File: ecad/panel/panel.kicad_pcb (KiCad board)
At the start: 4 copper layers, 165.5 x 51.6 mm, 200 parts, among them J2 Conn_01x03_Pin, J3 USB4105-GF-A, J4 5017868090, SW1 SW_SPDT, SW10 SW_SPDT, SW11 SW_SPDT, SW12 SW_SPDT, SW13 SW_SPDT, SW14 SW_SPDT, SW15 SW_SPDT, SW16 SW_SPDT, SW17 SW_Push, SW18 SW_Push, SW19 SW_Push, SW2 SW_SPDT, SW20 SW_Push, SW21 SW_Push, SW22 SW_Push, SW23 SW_Push, SW24 SW_Push, SW25 SW_Push, SW26 SW_Push, SW27 SW_Push, SW28 SW_Push, SW29 SW_Push, SW3 SW_SPDT, SW30 SW_Push, SW31 SW_Push, SW4 SW_SPDT, SW5 SW_SPDT, SW6 SW_SPDT, SW7 SW_SPDT, SW8 SW_SPDT, SW9 SW_SPDT, U1 TLC59211IN, U2 TLC59211IN, U3 TLC59211IN, U4 TLC59211IN, U5 TLC59211IN, U6 RP2350_80QFN, U7 W25Q128JVS, U8 MCP23017_SO, U9 MCP23017_SO, X1 ABM8-272-T3

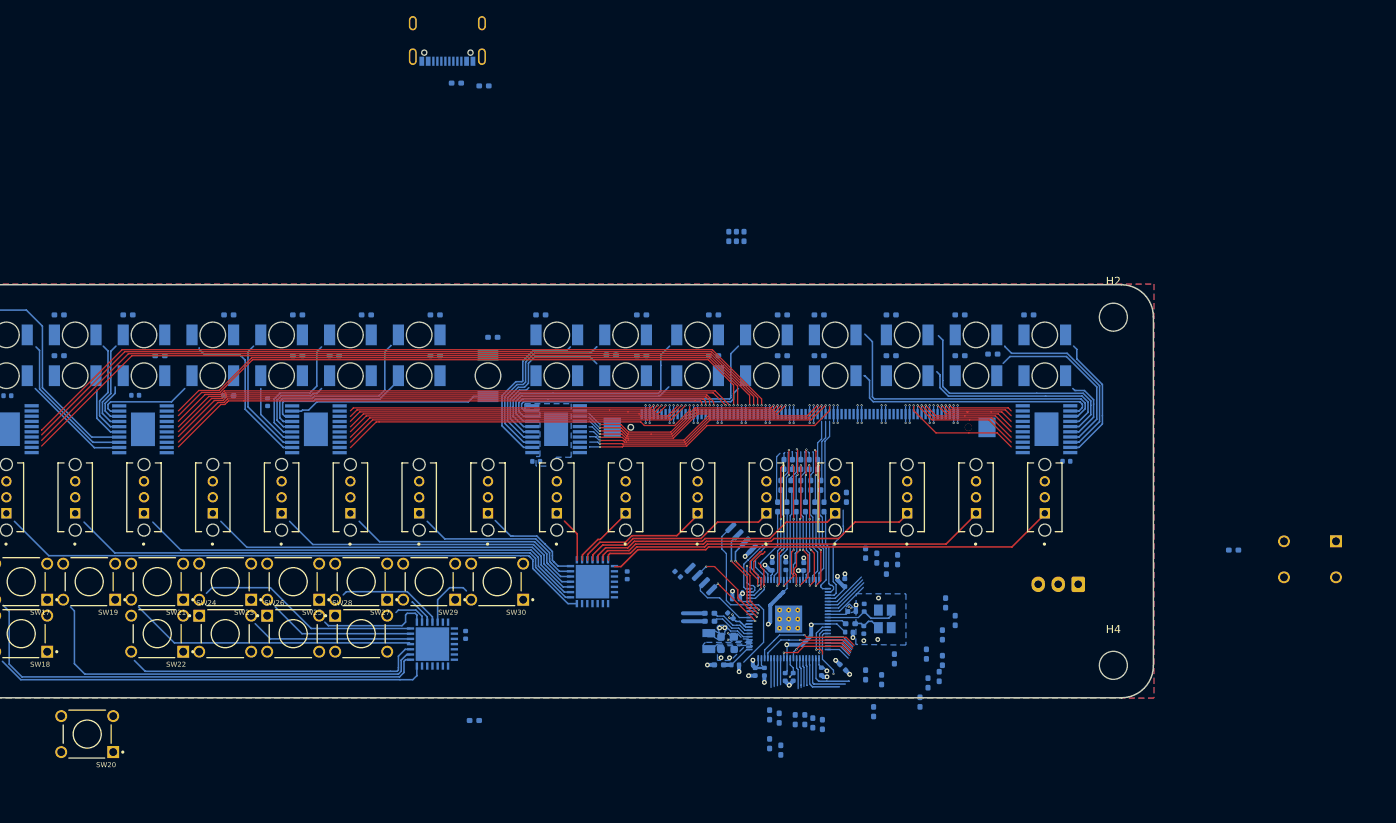
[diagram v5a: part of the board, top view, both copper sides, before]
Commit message: remap changes, various card panel fixes
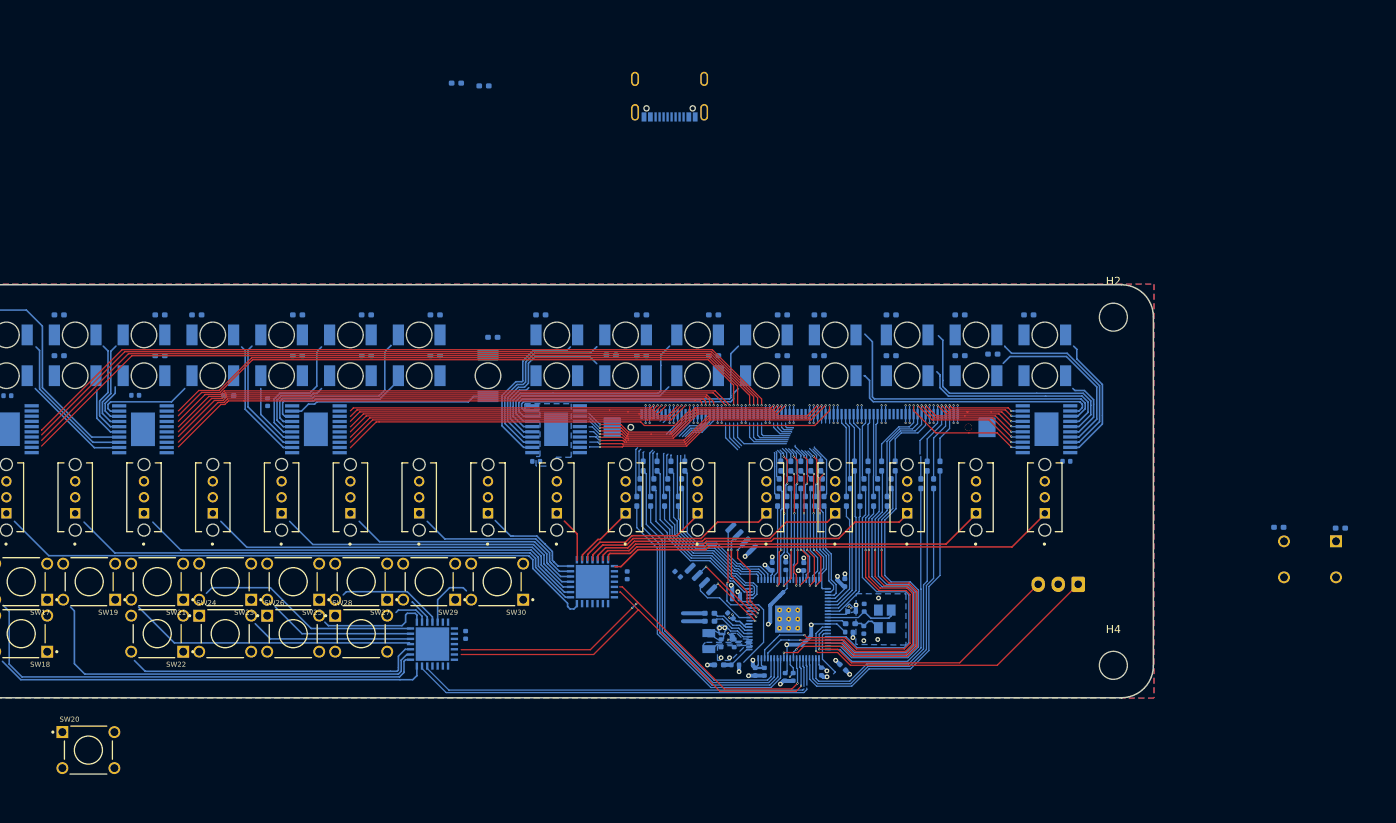
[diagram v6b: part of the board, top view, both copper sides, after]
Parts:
- C7, C8: footprint Capacitor_SMD:C_0603_1608Metric -> Capacitor_SMD:C_0402_1005Metric
- moved R25 110.9 mm to (224.6, 54.2)
- moved R84 37.7 mm to (137.0, 48.7)
- moved R80 36.1 mm to (139.1, 46.5)
- moved R85 35.8 mm to (137.4, 46.5)
- moved R77 35.8 mm to (140.5, 48.7)
- moved R79 35.0 mm to (138.7, 48.7)
- moved R83 34.6 mm to (136.6, 50.9)
- moved R46 33.9 mm to (141.8, 50.9)
- moved R78 33.3 mm to (140.1, 50.9)
- moved R47 31.9 mm to (142.2, 48.7)
- moved R76 31.8 mm to (174.5, 46.5)
- moved R86 30.6 mm to (138.3, 50.9)
- moved R45 29.6 mm to (140.9, 46.5)
- moved J3 28.6 mm to (140.7, -1.90)
- moved R75 27.4 mm to (173.7, 48.7)
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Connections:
- C10 pad 2: +1V1 -> GND
- C11 pad 2: +1V1 -> GND
- J4 pad 10: /BUS10 -> A1
- J4 pad 11: /BUS11 -> D1
- J4 pad 12: /BUS12 -> D0
- J4 pad 16: A0 -> /BUS16
- J4 pad 17: A1 -> /BUS17
- J4 pad 18: A2 -> /BUS18
- J4 pad 21: A3 -> /BUS21
- J4 pad 22: A4 -> /BUS22
- J4 pad 23: A5 -> /BUS23
- J4 pad 24: A6 -> /BUS24
- J4 pad 27: A7 -> /BUS27
- J4 pad 28: D0 -> /BUS28
- J4 pad 29: D1 -> /BUS29
- J4 pad 3: /BUS03 -> A3
- J4 pad 30: D2 -> /BUS30
- J4 pad 33: D3 -> D7
- J4 pad 34: D4 -> D6
- J4 pad 35: D5 -> A6
- J4 pad 36: D6 -> A7
- J4 pad 4: /BUS04 -> D3
- J4 pad 44: A8 -> A4
- J4 pad 45: A9 -> D4
- J4 pad 46: A10 -> A5
- J4 pad 47: A11 -> D5
- J4 pad 5: /BUS05 -> A2
- J4 pad 50: A12 -> PROT
- J4 pad 51: A13 -> INTE
- J4 pad 52: A14 -> WAIT
- J4 pad 53: A15 -> HLDA
- J4 pad 56: INT -> A12
- J4 pad 57: WO -> A13
- J4 pad 58: STACK -> OUT
- J4 pad 59: HLTA -> M1
- J4 pad 6: /BUS06 -> D2
- J4 pad 62: OUT -> A14
- J4 pad 63: M1 -> MEMR
- J4 pad 65: MEMR -> A15
- J4 pad 68: HLDA -> HLTA
- J4 pad 69: WAIT -> STACK
- J4 pad 70: PROT -> A11
- J4 pad 71: INTE -> WO
- J4 pad 74: I2C1_SCK -> A10
- J4 pad 75: I2C1_SDA -> INT
- J4 pad 76: I2C0_SCK -> A9
- J4 pad 77: I2C0_SDA -> A8
- J4 pad 9: /BUS09 -> A0
- R45 pad 2: INTE -> A14
- R46 pad 2: PROT -> MEMR
- R47 pad 2: WAIT -> INP
- R48 pad 2: HLDA -> A15
- R49 pad 2: MEMR -> HLTA
- R50 pad 2: INP -> STACK
- R51 pad 2: M1 -> A11
- R52 pad 2: OUT -> WO
- R53 pad 2: HLTA -> A10
- R54 pad 2: STACK -> INT
- R55 pad 2: WO -> A9
- R56 pad 2: INT -> A8
- R57 pad 2: A15 -> D7
- R58 pad 2: A14 -> D6
- R59 pad 2: A13 -> A6
- R60 pad 2: A12 -> A7
- R61 pad 2: A11 -> D5
- R62 pad 2: A10 -> D4
- R63 pad 2: A9 -> A5
- R64 pad 2: A8 -> A4
- R65 pad 2: D7 -> /BUS30
- R66 pad 2: D6 -> /BUS29
- R67 pad 2: D5 -> /BUS28
- R68 pad 2: D4 -> /BUS27
- R69 pad 2: D3 -> /BUS24
- R70 pad 2: D2 -> /BUS21
- R72 pad 2: D0 -> A0
- R73 pad 2: A7 -> D2
- R74 pad 2: A6 -> A2
- R75 pad 2: A5 -> D3
- R76 pad 2: A4 -> A3
- R77 pad 1: Net-(U6-GPIO36) -> Net-(U6-GPIO0)
- R77 pad 2: A3 -> M1
- R78 pad 1: Net-(U6-GPIO37) -> Net-(U6-GPIO1)
- R78 pad 2: A2 -> OUT
- R79 pad 1: Net-(U6-GPIO38) -> Net-(U6-GPIO2)
- R79 pad 2: A1 -> A12
- R80 pad 1: Net-(U6-GPIO39) -> Net-(U6-GPIO3)
- R80 pad 2: A0 -> A13
- R81 pad 2: /BUS15 -> D0
- R82 pad 2: /BUS12 -> A1
- R83 pad 2: /BUS11 -> PROT
- R84 pad 2: /BUS10 -> INTE
- R85 pad 2: /BUS09 -> WAIT
- R86 pad 2: /BUS06 -> HLDA
- R87 pad 2: /BUS05 -> /BUS22
- R88 pad 2: /BUS04 -> /BUS23
- U1 pad 6: HLDA -> PROT
- U1 pad 7: WAIT -> INTE
- U1 pad 8: PROT -> WAIT
- U1 pad 9: INTE -> HLDA
- U2 pad 2: INT -> A12
- U2 pad 3: WO -> A13
- U2 pad 4: STACK -> OUT
- U2 pad 5: HLTA -> M1
- U2 pad 6: OUT -> A14
- U2 pad 7: M1 -> MEMR
- U2 pad 9: MEMR -> A15
- U3 pad 4: A10 -> INT
- U3 pad 5: A11 -> A10
- U3 pad 6: A12 -> WO
- U3 pad 7: A13 -> A11
- U3 pad 8: A14 -> STACK
- U3 pad 9: A15 -> HLTA
- U4 pad 2: D0 -> A4
- U4 pad 3: D1 -> D4
- U4 pad 4: D2 -> A5
- U4 pad 5: D3 -> D5
- U4 pad 6: D4 -> A7
- U4 pad 7: D5 -> A6
- U5 pad 2: A0 -> D0
- U5 pad 3: A1 -> D1
- U5 pad 4: A2 -> A1
- U5 pad 5: A3 -> A0
- U5 pad 6: A4 -> D2
- U5 pad 7: A5 -> A2
- U5 pad 8: A6 -> D3
- U5 pad 9: A7 -> A3
- U6 pad 15: 3.3V -> GND
- U6 pad 24: 3.3V -> GND
- U6 pad 29: 3.3V -> GND
- U6 pad 41: 3.3V -> GND
- U6 pad 45: Net-(U6-GPIO36) -> unconnected-(U6-GPIO36-Pad45)
- U6 pad 46: Net-(U6-GPIO37) -> unconnected-(U6-GPIO37-Pad46)
- U6 pad 47: Net-(U6-GPIO38) -> I2C1_SDA
- U6 pad 48: Net-(U6-GPIO39) -> I2C1_SCK
- U6 pad 5: 3.3V -> GND
- U6 pad 50: 3.3V -> GND
- U6 pad 68: 3.3V -> GND
- U6 pad 69: 3.3V -> GND
- U6 pad 76: 3.3V -> GND
- U6 pad 77: I2C0_SDA -> Net-(U6-GPIO0)
- U6 pad 78: I2C0_SCK -> Net-(U6-GPIO1)
- U6 pad 79: I2C1_SDA -> Net-(U6-GPIO2)
- U6 pad 80: I2C1_SCK -> Net-(U6-GPIO3)
- U8 pad 12: I2C0_SCK -> /I2C0_SCK
- U8 pad 13: I2C0_SDA -> /I2C0_SDA
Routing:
- net I2C1_SDA: track 44.2 -> 95.8 mm
- net unconnected-(U8-INTA-Pad20): track 0.00 -> 50.0 mm
- net unconnected-(U8-INTB-Pad19): track 0.00 -> 48.6 mm
- net I2C1_SCK: track 48.4 -> 96.1 mm, vias 1 -> 4
- net I2C0_SCK: track 46.4 -> 0.00 mm, vias 2 -> 0
- net I2C0_SDA: track 45.2 -> 0.00 mm, vias 2 -> 0
- net (no net): track 0.00 -> 39.0 mm, vias 0 -> 1
- net A6: track 0.00 -> 37.5 mm, vias 0 -> 2
- net Net-(U6-GPIO44_ADC4): track 3.54 -> 40.3 mm
- net Net-(J2-Pin_1): track 5.04 -> 41.7 mm
- net D7: track 0.00 -> 36.3 mm, vias 0 -> 2
- net Net-(U6-GPIO43_ADC3): track 3.42 -> 39.3 mm
- net Net-(U6-GPIO35): track 7.08 -> 42.8 mm
- net Net-(U6-GPIO31): track 3.15 -> 38.3 mm
- net A4: track 0.00 -> 34.9 mm, vias 0 -> 2
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
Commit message: near-final panel routing
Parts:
- removed the SW20 at (68.0, 82.0)
- added C28: 10u, Capacitor_SMD:C_0402_1005Metric, F.Cu at (102.4, 16.1)
- added C29: 10u, Capacitor_SMD:C_0402_1005Metric, F.Cu at (102.4, 18.1)
- added D37: DEBUG, Diode_SMD:D_0402_1005Metric_Pad0.77x0.64mm_HandSolder, F.Cu at (105.7, 16.1)
- added D41: D_Schottky, Diode_SMD:D_0402_1005Metric, F.Cu at (109.0, 16.1)
- added U10: NCP1117-3.3_SOT223, Package_TO_SOT_SMD:SOT-223-3_TabPin2, B.Cu at (179.0, 61.4)
- moved J2 88.6 mm to (105.2, 42.4), turned to 0 degrees
- moved R16 1.20 mm to (54.6, 37.7), turned to 0 degrees
- moved C10 0.76 mm to (155.2, 72.1), turned to -90 degrees
- moved C16 0.75 mm to (156.1, 72.1)
- moved C1 0.73 mm to (57.2, 37.8)
- moved R8 0.71 mm to (132.7, 32.7)
- renumbered SW21 to SW20, SW22 to SW21, SW23 to SW22, SW24 to SW23, SW25 to SW24, SW26 to SW25, SW27 to SW26, SW28 to SW27, SW29 to SW28, SW30 to SW29, SW31 to SW30
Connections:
- D29 pad 1: /MI_LED -> /M1_LED
- J4 pad 44: A4 -> D5
- J4 pad 45: D4 -> A5
- J4 pad 46: A5 -> D4
- J4 pad 47: D5 -> A4
- R45 pad 2: A14 -> A15
- R46 pad 2: MEMR -> INP
- R47 pad 2: INP -> MEMR
- R48 pad 2: A15 -> A14
- R49 pad 2: HLTA -> M1
- R50 pad 2: STACK -> OUT
- R51 pad 2: A11 -> A13
- R52 pad 2: WO -> HLDA
- R53 pad 2: A10 -> A12
- R54 pad 2: INT -> WAIT
- R55 pad 2: A9 -> INTE
- R56 pad 2: A8 -> PROT
- R57 pad 2: D7 -> A4
- R58 pad 2: D6 -> D4
- R59 pad 2: A6 -> A5
- R60 pad 2: A7 -> D5
- R61 pad 2: D5 -> A7
- R62 pad 2: D4 -> D6
- R63 pad 2: A5 -> A6
- R64 pad 2: A4 -> D7
- R77 pad 2: M1 -> HLTA
- R78 pad 2: OUT -> STACK
- R79 pad 2: A12 -> WO
- R80 pad 2: A13 -> A11
- R83 pad 2: PROT -> A8
- R84 pad 2: INTE -> A9
- R85 pad 2: WAIT -> INT
- R86 pad 2: HLDA -> A10
- SW19 pad 2: SINGLE -> SINGLE_STEP
- U1 pad 12: /PROT_LED -> /HDLA_LED
- U1 pad 13: /INTE_LED -> /WAIT_LED
- U1 pad 14: /WAIT_LED -> /INTE_LED
- U1 pad 15: /HDLA_LED -> /PROT_LED
- U2 pad 12: /MEMR_LED -> /A15_LED
- U2 pad 14: /MI_LED -> /MEMR_LED
- U2 pad 15: /OUT_LED -> /A14_LED
- U2 pad 16: /HLTA_LED -> /M1_LED
- U2 pad 17: /STACK_LED -> /OUT_LED
- U2 pad 18: /WO_LED -> /A13_LED
- U2 pad 19: /INT_LED -> /A12_LED
- U3 pad 12: /A15_LED -> /HLTA_LED
- U3 pad 13: /A14_LED -> /STACK_LED
- U3 pad 14: /A13_LED -> /A11_LED
- U3 pad 15: /A12_LED -> /WO_LED
- U3 pad 16: /A11_LED -> /A10_LED
- U3 pad 17: /A10_LED -> /INT_LED
- U4 pad 14: /D5_LED -> /A6_LED
- U4 pad 15: /D4_LED -> /A7_LED
- U4 pad 16: /D3_LED -> /D5_LED
- U4 pad 17: /D2_LED -> /A5_LED
- U4 pad 18: /D1_LED -> /D4_LED
- U4 pad 19: /D0_LED -> /A4_LED
- U5 pad 12: /A7_LED -> /A3_LED
- U5 pad 13: /A6_LED -> /D3_LED
- U5 pad 14: /A5_LED -> /A2_LED
- U5 pad 15: /A4_LED -> /D2_LED
- U5 pad 16: /A3_LED -> /A0_LED
- U5 pad 17: /A2_LED -> /A1_LED
- U5 pad 18: /A1_LED -> /D1_LED
- U5 pad 19: /A0_LED -> /D0_LED
- U8 pad 1: A15_SW -> CLR
- U8 pad 12: /I2C0_SCK -> I2C1_SCK
- U8 pad 13: /I2C0_SDA -> I2C1_SDA
- U8 pad 19: unconnected-(U8-INTB-Pad19) -> /PUSH_INTB
- U8 pad 2: A14_SW -> UNPROTECT
- U8 pad 20: unconnected-(U8-INTA-Pad20) -> /PUSH_INTA
- U8 pad 21: DEPOSIT -> RUN
- U8 pad 22: DEPOSIT_NEXT -> STOP
- U8 pad 23: EXAMINE -> SINGLE_STEP
- U8 pad 25: STEP -> EXAMINE
- U8 pad 26: SINGLE -> DEPOSIT_NEXT
- U8 pad 27: RUN -> RESET
- U8 pad 28: STOP -> DEPOSIT
- U8 pad 3: A13_SW -> AUX1
- U8 pad 4: A12_SW -> PROTECT
- U8 pad 5: A11_SW -> AUX2
- U8 pad 6: A10_SW -> unconnected-(U8-GPB5-Pad6)
- U8 pad 7: A9_SW -> unconnected-(U8-GPB6-Pad7)
- U8 pad 8: A8_SW -> unconnected-(U8-GPB7-Pad8)
- U9 pad 21: AUX2 -> A15_SW
- U9 pad 22: AUX1 -> A14_SW
- U9 pad 23: UNPROTECT -> A13_SW
- U9 pad 24: PROTECT -> A12_SW
- U9 pad 25: CLR -> A11_SW
- U9 pad 26: RESET -> A10_SW
- U9 pad 27: unconnected-(U9-GPA6-Pad27) -> A9_SW
- U9 pad 28: unconnected-(U9-GPA7-Pad28) -> A8_SW
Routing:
- net AUX2: track 76.2 -> 7.91 mm
- net INTE: track 46.2 -> 112.5 mm, vias 1 -> 4
- net A15_SW: track 13.8 -> 77.6 mm
- net WAIT: track 45.0 -> 107.8 mm, vias 1 -> 2
- net A14_SW: track 4.44 -> 66.9 mm
- net PROT: track 49.3 -> 110.4 mm, vias 1 -> 2
- net AUX1: track 65.4 -> 4.58 mm
- net HLDA: track 51.4 -> 109.7 mm, vias 1 -> 2
- net A13_SW: track 3.33 -> 58.0 mm
- net SINGLE_STEP: track 0.00 -> 53.0 mm
- net UNPROTECT: track 56.5 -> 5.71 mm
- net unconnected-(U8-INTA-Pad20): track 50.0 -> 0.00 mm
- net /PUSH_INTA: track 0.00 -> 50.0 mm
- net unconnected-(U8-INTB-Pad19): track 48.6 -> 0.00 mm
- net /PUSH_INTB: track 0.00 -> 48.6 mm
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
